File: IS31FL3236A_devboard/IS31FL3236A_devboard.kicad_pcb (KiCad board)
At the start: 2 copper layers, 20.3 x 61 mm, 46 parts, among them J1 Conn_01x24, J2 Conn_01x24, U1 IS31FL3236-TQ

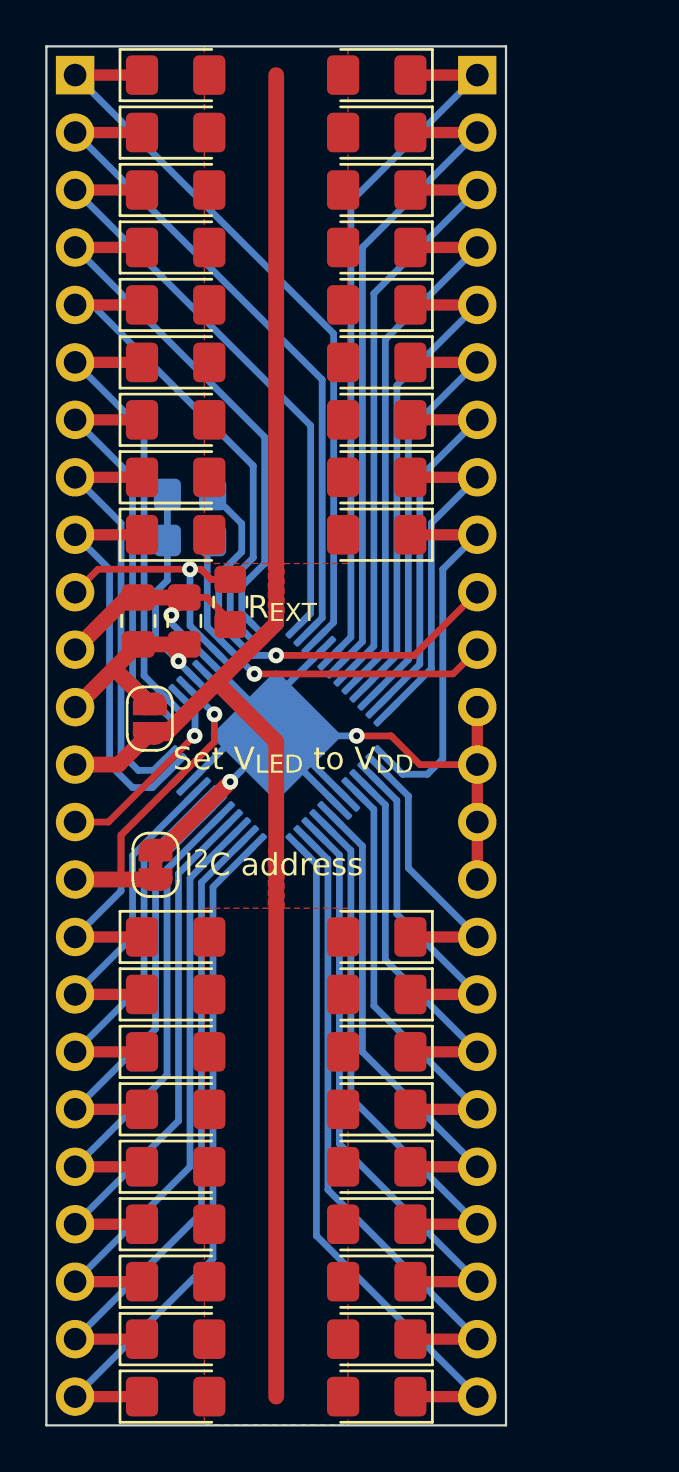
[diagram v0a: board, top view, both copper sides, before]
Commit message: LED driver devboeard
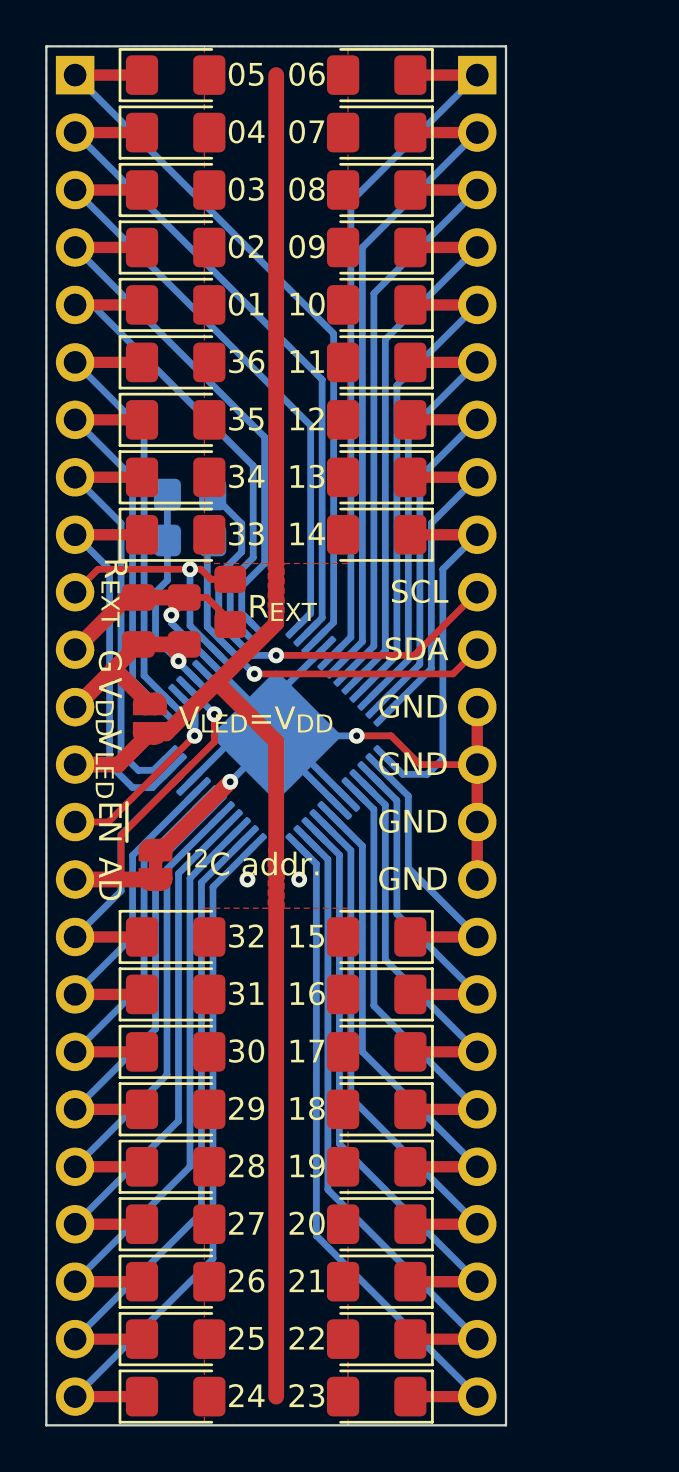
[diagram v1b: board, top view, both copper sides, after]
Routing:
- net GND: vias 3 -> 5
- added copper zone on B.Cu, net GND
- added copper zone on F.Cu, net GND
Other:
- board text added: "01"
- board text added: "02"
- board text added: "03"
- board text added: "04"
- board text added: "05"
- board text added: "06"
- board text added: "07"
- board text added: "08"
- board text added: "09"
- board text added: "10"
- board text added: "11"
- board text added: "12"
- board text added: "13"
- board text added: "14"
- board text added: "15"
- board text added: "16"
- board text added: "17"
- board text added: "18"
- board text added: "19"
- board text added: "20"
- board text added: "21"
- board text added: "22"
- board text added: "23"
- board text added: "24"
- board text added: "25"
- board text added: "26"
- board text added: "27"
- board text added: "28"
- board text added: "29"
- board text added: "30"
- board text added: "31"
- board text added: "32"
- board text added: "33"
- board text added: "34"
- board text added: "35"
- board text added: "36"
- board text added: "AD"
- board text added: "G"
- board text added: "GND"
- board text added: "I^{2}C addr."
- board text added: "SCL"
- board text added: "SDA"
- board text added: "V_{DD}"
- board text added: "V_{LED}"
- board text added: "V_{LED}=V_{DD}"
- board text added: "~{EN}"
- board text removed: "I^{2}C address"
- board text removed: "Set V_{LED} to V_{DD}"
